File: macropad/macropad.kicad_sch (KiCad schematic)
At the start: 0 parts

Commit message: Add rotary_encoder submodule
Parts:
- added D1, D10, D11, D12, D2, D3, D4, D5, D6, D7, D8, D9: 1N4148, Diode_THT:D_DO-35_SOD27_P7.62mm_Horizontal, symbol Diode:1N4148
- added SW1, SW10, SW11, SW12, SW2, SW3, SW4, SW5, SW6, SW7, SW8, SW9: SW_Push, Button_Switch_Keyboard:SW_Cherry_MX_1.00u_PCB, symbol Switch:SW_Push
- added SW13: RotaryEncoder_Switch, symbol Device:RotaryEncoder_Switch
- added U1: MOUDLE-SEEEDUINO-XIAO, footprints:XIAO-Generic-Hybrid-14P-2.54-21X17.8MM, symbol XIAO_RP2040:MOUDLE-SEEEDUINO-XIAO
- added U2: ER_OLEDM0.91_1x-I2C, Display:ER_OLEDM0.91_1x-I2C, symbol Display_Graphic:ER_OLEDM0.91_1x-I2C
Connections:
- new net: D7.2 (A), SW7.2
- new net: D8.2 (A), SW8.2
- new net: D5.2 (A), SW5.2
- new net: D9.2 (A), SW9.2
- new net: D4.2 (A), SW4.2
- new net: D3.2 (A), SW3.2
- new net: D12.2 (A), SW12.2
- new net: D1.2 (A), SW1.2
- new net: D2.2 (A), SW2.2
- new net: D6.2 (A), SW6.2
- new net: D11.2 (A), SW11.2
- new net: SW13.A, U1.9 (PA7_A8_D8_SCK)
- new net: SW13.B, U1.8 (PB09_A7_D7_RX)
- new net: D10.2 (A), SW10.2
- new net: U1.6 (PA9_A5_D5_SCL), U2.3 (SCL)
- new net: U1.5 (PA8_A4_D4_SDA), U2.4 (SDA)
- new net Col 0: SW1.1, SW5.1, SW9.1, U1.4 (PA11_A3_D3)
- new net Col 1: SW10.1, SW2.1, SW6.1, U1.11 (PA6_A10_D10_MOSI)
- new net Col 2: SW11.1, SW3.1, SW7.1, U1.10 (PA5_A9_D9_MISO)
- new net Col 3: SW12.1, SW4.1, SW8.1, U1.7 (PB08_A6_D6_TX)
- new net GND: SW13.C, U1.13 (GND), U2.1 (GND)
- new net Row 0: D1.1 (K), D2.1 (K), D3.1 (K), D4.1 (K), U1.1 (PA02_A0_D0)
- new net Row 1: D5.1 (K), D6.1 (K), D7.1 (K), D8.1 (K), U1.2 (PA4_A1_D1)
- new net Row 2: D10.1 (K), D11.1 (K), D12.1 (K), D9.1 (K), U1.3 (PA10_A2_D2)
- new net VCC: U1.12 (3V3), U2.2 (VCC)

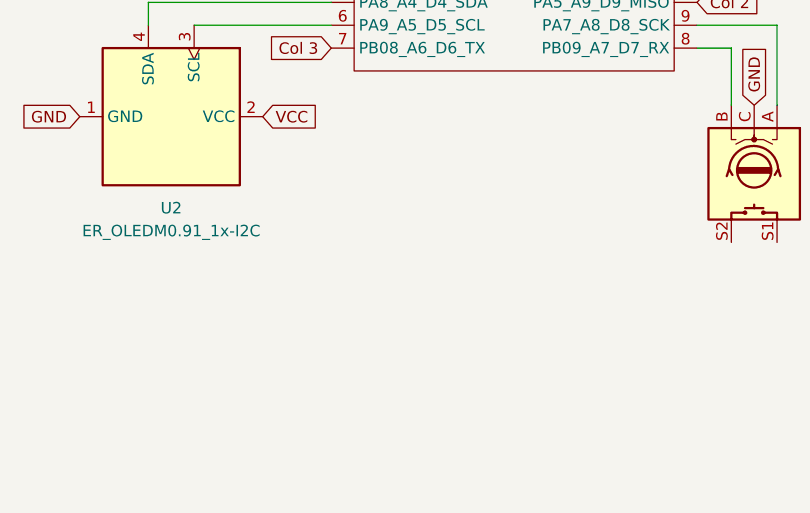
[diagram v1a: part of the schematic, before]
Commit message: Footprint edits
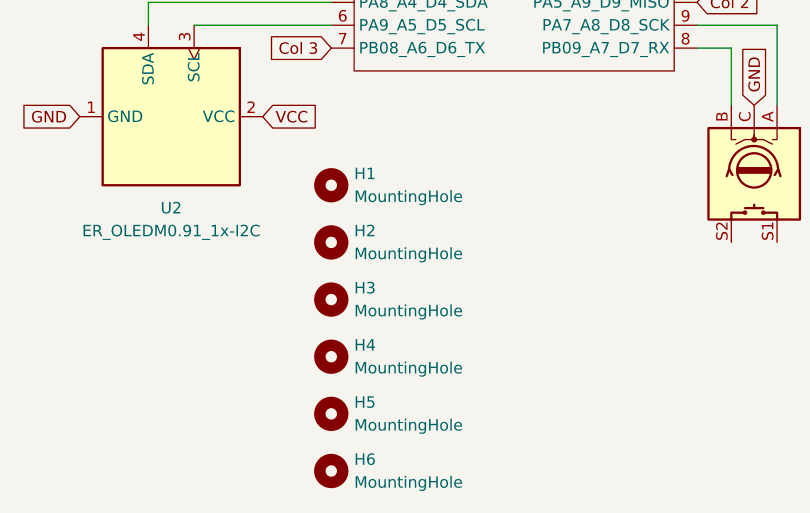
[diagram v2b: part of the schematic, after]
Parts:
- added H1, H2, H3, H4, H5, H6: MountingHole, MountingHole:MountingHole_3.2mm_M3, symbol Mechanical:MountingHole
- SW13: footprint (none) -> Rotary_Encoder:RotaryEncoder_Alps_EC11E-Switch_Vertical_H20mm

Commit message: Add rotary encoder step file
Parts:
- SW1, SW10, SW11, SW12, SW2, SW3, SW4, SW5, SW6, SW7, SW8, SW9: footprint Button_Switch_Keyboard:SW_Cherry_MX_1.00u_PCB -> footprints:SW_Cherry_MX_1.00u_PCB_(3D_STEP)
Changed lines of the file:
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@@
 			)
 		)
-		(property "Footprint" "Button_Switch_Keyboard:SW_Cherry_MX_1.00u_PCB"
+		(property "Footprint" "footprints:SW_Cherry_MX_1.00u_PCB_(3D_STEP)"
 			(at 107.95 80.01 0)
 			(hide yes)
@@
 			)
 		)
-		(property "Footprint" "Button_Switch_Keyboard:SW_Cherry_MX_1.00u_PCB"
+		(property "Footprint" "footprints:SW_Cherry_MX_1.00u_PCB_(3D_STEP)"
 			(at 129.54 99.06 0)
 			(hide yes)
@@
 			)
 		)
-		(property "Footprint" "Button_Switch_Keyboard:SW_Cherry_MX_1.00u_PCB"
+		(property "Footprint" "footprints:SW_Cherry_MX_1.00u_PCB_(3D_STEP)"
 			(at 64.77 62.23 0)
 			(hide yes)
@@
 			)
 		)
-		(property "Footprint" "Button_Switch_Keyboard:SW_Cherry_MX_1.00u_PCB"
+		(property "Footprint" "footprints:SW_Cherry_MX_1.00u_PCB_(3D_STEP)"
 			(at 86.36 62.23 0)
 			(hide yes)
@@
 			)
 		)
-		(property "Footprint" "Button_Switch_Keyboard:SW_Cherry_MX_1.00u_PCB"
+		(property "Footprint" "footprints:SW_Cherry_MX_1.00u_PCB_(3D_STEP)"
 			(at 86.36 80.01 0)
 			(hide yes)
@@
 			)
 		)
-		(property "Footprint" "Button_Switch_Keyboard:SW_Cherry_MX_1.00u_PCB"
+		(property "Footprint" "footprints:SW_Cherry_MX_1.00u_PCB_(3D_STEP)"
 			(at 129.54 62.23 0)
 			(hide yes)
@@
 			)
 		)
-		(property "Footprint" "Button_Switch_Keyboard:SW_Cherry_MX_1.00u_PCB"
+		(property "Footprint" "footprints:SW_Cherry_MX_1.00u_PCB_(3D_STEP)"
 			(at 107.95 99.06 0)
 			(hide yes)
@@
 			)
 		)
-		(property "Footprint" "Button_Switch_Keyboard:SW_Cherry_MX_1.00u_PCB"
+		(property "Footprint" "footprints:SW_Cherry_MX_1.00u_PCB_(3D_STEP)"
 			(at 129.54 80.01 0)
 			(hide yes)
@@
 			)
 		)
-		(property "Footprint" "Button_Switch_Keyboard:SW_Cherry_MX_1.00u_PCB"
+		(property "Footprint" "footprints:SW_Cherry_MX_1.00u_PCB_(3D_STEP)"
 			(at 107.95 62.23 0)
 			(hide yes)
@@
 			)
 		)
-		(property "Footprint" "Button_Switch_Keyboard:SW_Cherry_MX_1.00u_PCB"
+		(property "Footprint" "footprints:SW_Cherry_MX_1.00u_PCB_(3D_STEP)"
 			(at 64.77 80.01 0)
 			(hide yes)
@@
 			)
 		)
-		(property "Footprint" "Button_Switch_Keyboard:SW_Cherry_MX_1.00u_PCB"
+		(property "Footprint" "footprints:SW_Cherry_MX_1.00u_PCB_(3D_STEP)"
 			(at 64.77 99.06 0)
 			(hide yes)
@@
 			)
 		)
-		(property "Footprint" "Button_Switch_Keyboard:SW_Cherry_MX_1.00u_PCB"
+		(property "Footprint" "footprints:SW_Cherry_MX_1.00u_PCB_(3D_STEP)"
 			(at 86.36 99.06 0)
 			(hide yes)

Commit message: Add Xiao and OLED STEP file
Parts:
- U2: footprint Display:ER_OLEDM0.91_1x-I2C -> footprints:ER_OLEDM0.91_1x-I2C_(3D_STEP)
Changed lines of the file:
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@@
 			)
 		)
-		(property "Footprint" "Display:ER_OLEDM0.91_1x-I2C"
+		(property "Footprint" "footprints:ER_OLEDM0.91_1x-I2C_(3D_STEP)"
 			(at 63.5 165.354 0)
 			(hide yes)
